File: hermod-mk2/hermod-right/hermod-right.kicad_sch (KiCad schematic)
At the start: 41 parts, among them J1 USB_C_Receptacle_USB2.0, J2 Conn_01x05, J3 USB_C_Receptacle_USB2.0, Q1 AO3401A, Q2 MMUN2233LT1G, U2 PRTR5V0U2X, U3 XC6206PxxxMR-Regulator_Linear, U4 CR2013-MI2120, U5 TXB0101, U8 STM32G474RETx

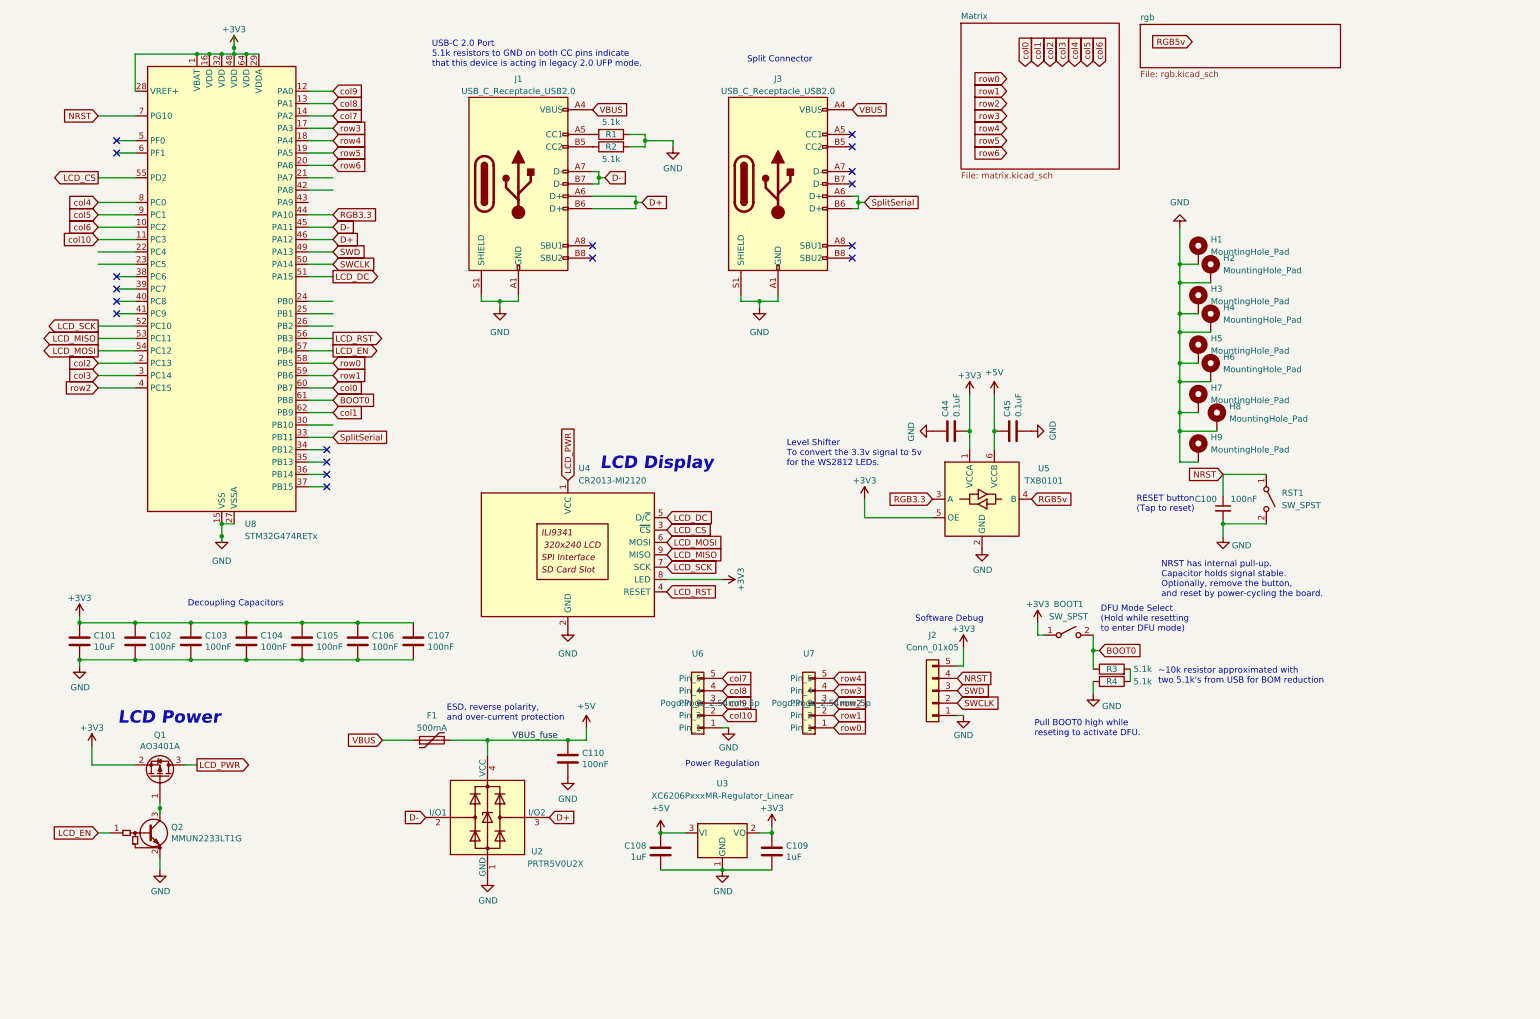
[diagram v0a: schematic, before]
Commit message: Fixed up the 5v for LEDs
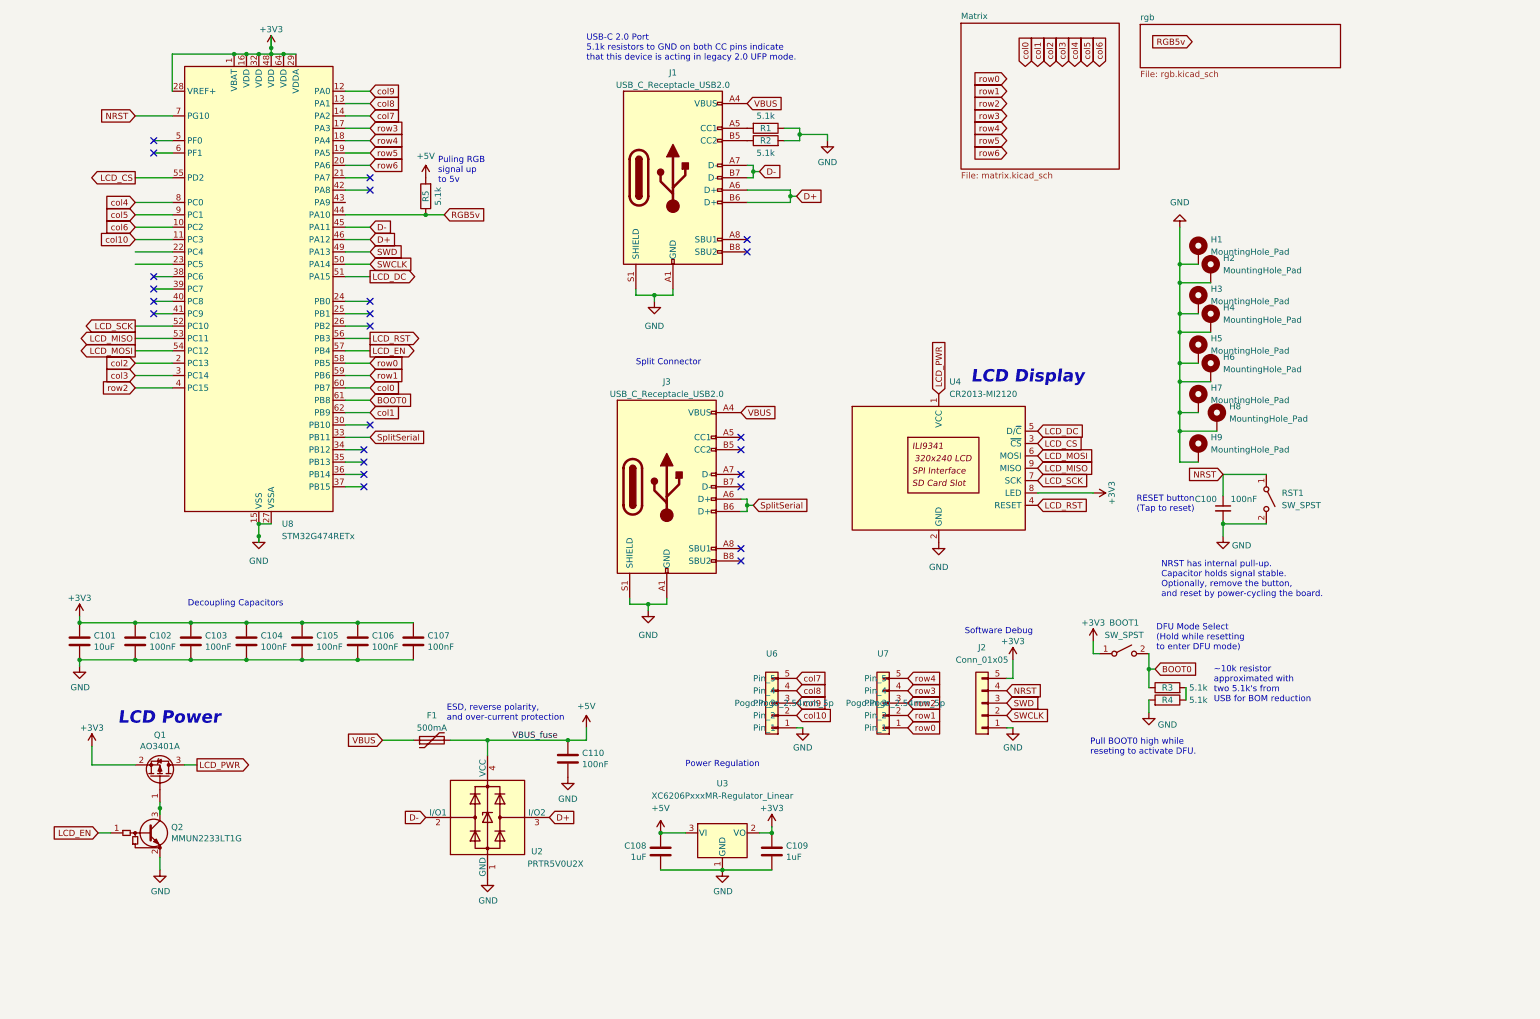
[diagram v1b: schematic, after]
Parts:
- removed C44, C45: 0.1uF, Capacitor_SMD:C_0402_1005Metric, symbol Device:C
- removed U5: TXB0101, Package_TO_SOT_SMD:SOT-363_SC-70-6_Handsoldering, symbol PCM_marbastlib-various:TXB0101
- added R5: 5.1k, Resistor_SMD:R_0402_1005Metric, symbol Device:R
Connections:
- net RGB3.3 is gone; now on net RGB5v: U8.44 (PA10)
- net +5V: now also R5.2
- net RGB5v: now also R5.1
- no-connect marks 18 -> 24
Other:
- note added: "Puling RGB signal up to 5v"
- note removed: "Level Shifter To convert the 3.3v signal to 5v for the WS2812 LEDs."
- moved on the sheet: BOOT1, J1, J2, J3, R1, R2, R3, R4, U4, U6, U7, U8

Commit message: Fixed up hermod mk1 and updated hermod mk2
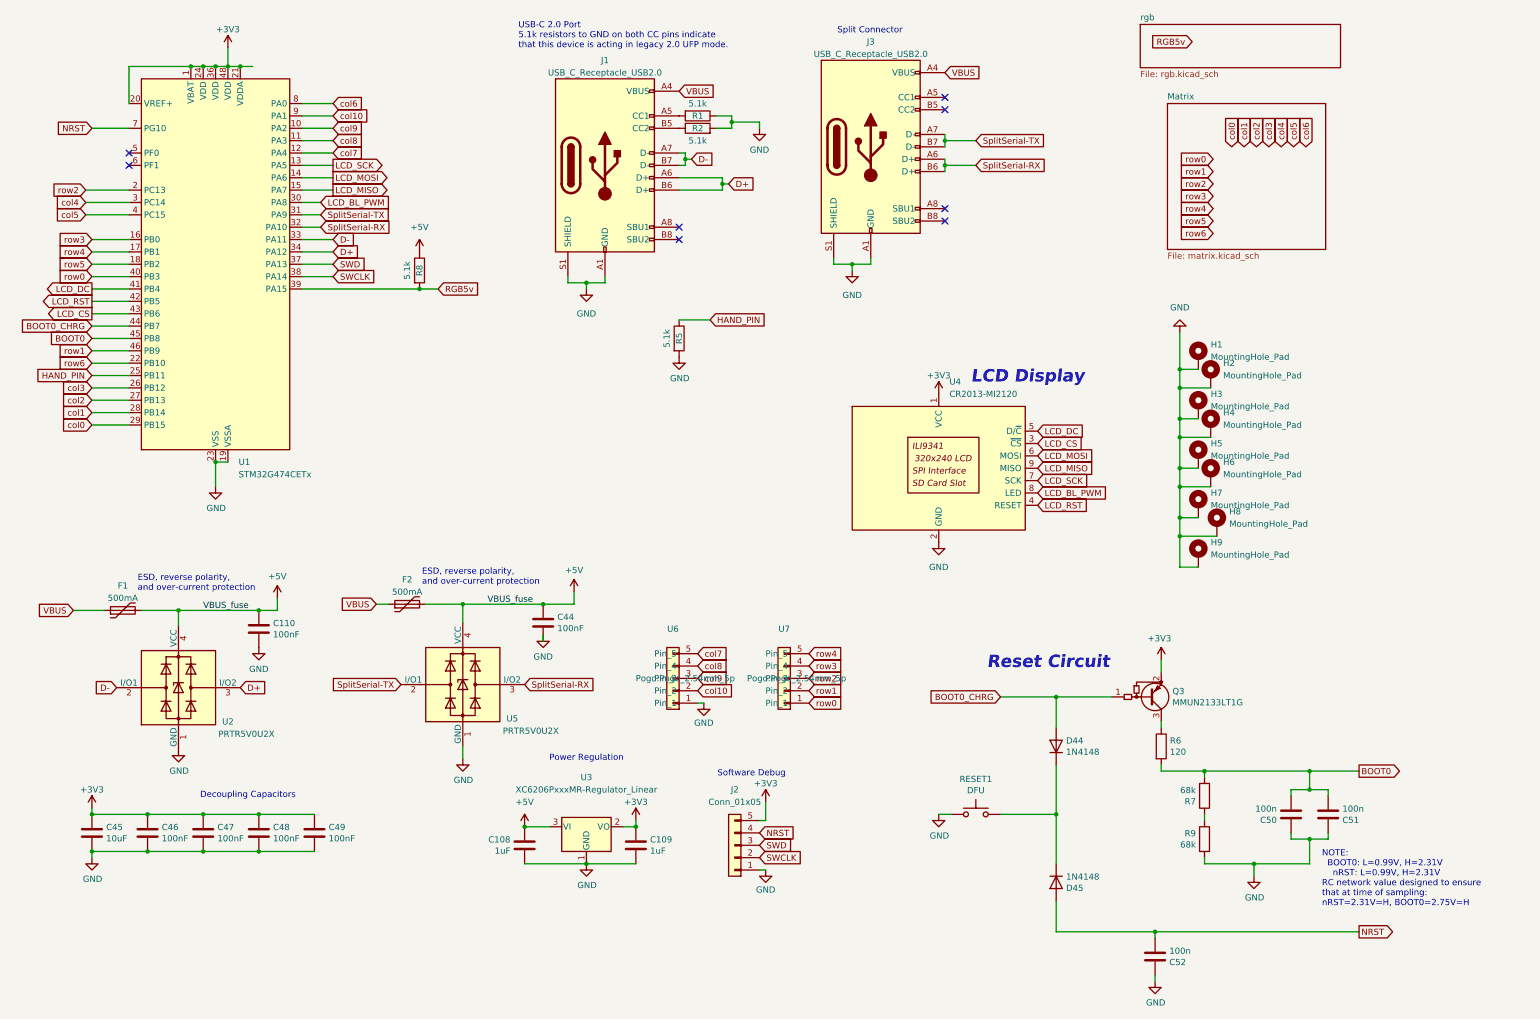
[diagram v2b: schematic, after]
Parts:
- removed BOOT1, RST1: SW_SPST, Button_Switch_SMD:SW_SPST_TL3342, symbol Switch:SW_SPST
- removed C100: 100nF, Capacitor_SMD:C_0402_1005Metric, symbol Device:C_Small
- removed C101: 10uF, Capacitor_SMD:C_0603_1608Metric, symbol Device:C
- removed C102, C103, C104, C105, C106, C107: 100nF, Capacitor_SMD:C_0402_1005Metric, symbol Device:C
- removed Q1: AO3401A, Package_TO_SOT_SMD:SOT-23-3, symbol Transistor_FET:AO3401A
- removed Q2: MMUN2233LT1G, Package_TO_SOT_SMD:SOT-23-3, symbol Device:Q_NPN_BEC_BRT
- removed R3, R4: 5.1k, Resistor_SMD:R_0402_1005Metric, symbol Device:R
- removed U8: STM32G474RETx, Package_QFP:LQFP-64_10x10mm_P0.5mm, symbol MCU_ST_STM32G4:STM32G474RETx
- added C44, C46, C47, C48, C49: 100nF, Capacitor_SMD:C_0402_1005Metric, symbol Device:C
- added C45: 10uF, Capacitor_SMD:C_0603_1608Metric, symbol Device:C
- added C50, C51, C52: 100n, Capacitor_SMD:C_0805_2012Metric, symbol Device:C
- added D44, D45: 1N4148, Diode_SMD:D_SOD-123, symbol Device:D
- added F2: 500mA, Fuse:Fuse_1206_3216Metric, symbol Device:Polyfuse
- added Q3: MMUN2133LT1G, Package_TO_SOT_SMD:SOT-23-3, symbol Device:Q_PNP_BEC_BRT
- added R6: 120, Resistor_SMD:R_0805_2012Metric, symbol Device:R
- added R7, R9: 68k, Resistor_SMD:R_0805_2012Metric, symbol Device:R
- added R8: 5.1k, Resistor_SMD:R_0402_1005Metric, symbol Device:R
- added RESET1: DFU, Button_Switch_SMD:SW_SPST_TL3342, symbol Switch:SW_Push
- added U1: STM32G474CETx, Package_QFP:LQFP-48_7x7mm_P0.5mm, symbol MCU_ST_STM32G4:STM32G474CETx
- added U5: PRTR5V0U2X, Package_TO_SOT_SMD:SOT-143, symbol Power_Protection:PRTR5V0U2X
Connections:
- net LCD_PWR is gone; now on net +3V3: U4.1 (VCC)
- net +3V3: now also C45.1, C46.1, C47.1, C48.1, C49.1, Q3.2 (E), U1.1 (VBAT), U1.20 (VREF+), U1.21 (VDDA), U1.24 (VDD), U1.36 (VDD), U1.48 (VDD); no longer U4.8 (LED)
- net +5V: now also C44.1, F2.2, R8.1, U5.4 (VCC); no longer R5.2
- net BOOT0: now also C50.2, C51.2, R6.2, R7.2, U1.45 (PB8)
- net D+: now also U1.34 (PA12)
- net D-: now also U1.33 (PA11)
- net GND: now also R5.2, C44.2, C45.2, C46.2, C47.2, C48.2, C49.2, C50.1, C51.1, C52.1, R9.2, RESET1.1, U1.19 (VSSA), U1.23 (VSS), U1.35 (VSS), U1.47 (VSS), U5.1 (GND)
- net LCD_CS: now also U1.43 (PB6)
- net LCD_DC: now also U1.41 (PB4)
- net LCD_MISO: now also U1.15 (PA7)
- net LCD_MOSI: now also U1.14 (PA6)
- net LCD_RST: now also U1.42 (PB5)
- net LCD_SCK: now also U1.13 (PA5)
- net NRST: now also C52.2, D45.2 (A), U1.7 (PG10)
- net RGB5v: now also R8.2, U1.39 (PA15); no longer R5.1
- net SWCLK: now also U1.38 (PA14)
- net SWD: now also U1.37 (PA13)
- net VBUS: now also F2.1
- net col0: now also U1.29 (PB15)
- net col1: now also U1.28 (PB14)
- net col10: now also U1.9 (PA1)
- net col2: now also U1.27 (PB13)
- net col3: now also U1.26 (PB12)
- net col4: now also U1.3 (PC14)
- net col5: now also U1.4 (PC15)
- net col6: now also U1.8 (PA0)
- net col7: now also U1.12 (PA4)
- net col8: now also U1.11 (PA3)
- net col9: now also U1.10 (PA2)
- net row0: now also U1.40 (PB3)
- net row1: now also U1.46 (PB9)
- net row2: now also U1.2 (PC13)
- net row3: now also U1.16 (PB0)
- net row4: now also U1.17 (PB1)
- net row5: now also U1.18 (PB2)
- net row6: now also U1.22 (PB10)
- net SplitSerial-TX: now reaches J3.A7 (D-)
- net SplitSerial-TX: now also J3.B7 (D-), U1.31 (PA9), U5.2 (I/O1)
- net SplitSerial renamed SplitSerial-RX
- net SplitSerial-RX: now also U1.32 (PA10), U5.3 (I/O2)
- new net: Q3.3 (C), R6.1
- new net: R7.1, R9.1
- new net: D44.1 (K), D45.1 (K), RESET1.2
- new net BOOT0_CHRG: D44.2 (A), Q3.1 (B), U1.44 (PB7)
- new net HAND_PIN: R5.1, U1.25 (PB11)
- new net LCD_BL_PWM: U1.30 (PA8), U4.8 (LED)
- no-connect marks 24 -> 8
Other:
- note added: "NOTE: BOOT0: L=0.99V, H=2.31V nRST: L=0.99V, H=2.31V RC network value designed to ensure that at time of sampling: nRST=2.31V=H, BOOT0=2.75V=H"
- note added: "Reset Circuit"
- note removed: "DFU Mode Select (Hold while resetting to enter DFU mode)"
- note removed: "LCD Power"
- note removed: "NRST has internal pull-up. Capacitor holds signal stable. Optionally, remove the button, and reset by power-cycling the board."
- note removed: "Puling RGB signal up to 5v"
- note removed: "Pull BOOT0 high while reseting to activate DFU."
- note removed: "RESET button (Tap to reset)"
- note removed: "~10k resistor approximated with two 5.1k's from USB for BOM reduction"
- moved on the sheet: C108, C109, C110, F1, H1, H2, H3, H4, H5, H6, H7, H8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
